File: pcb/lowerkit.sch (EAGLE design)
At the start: 28 parts, among them IC1 MC6847, IC3 74LS93N, IC4 74LS04N, IC5 74LS125N, IC6 74LS86N, IC7 74LS73N, IC8 74LS157N, IC9 74LS157N

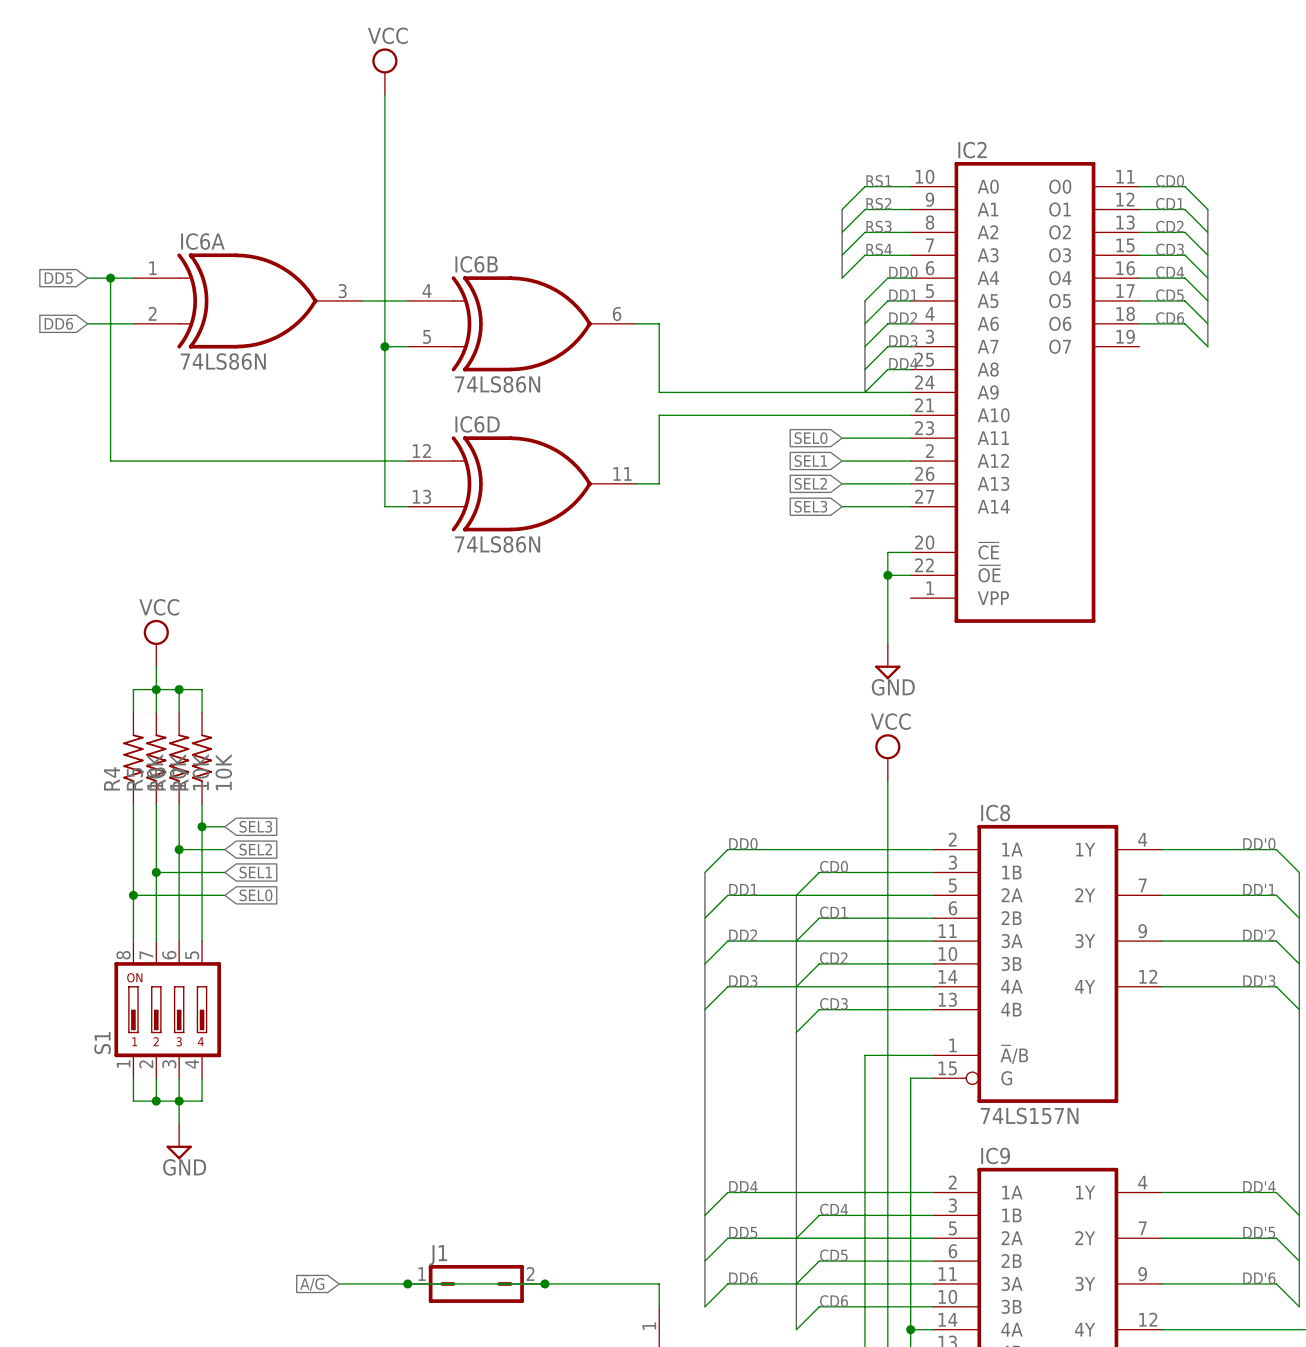
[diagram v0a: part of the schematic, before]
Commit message: Converted original design back to 2716 usage
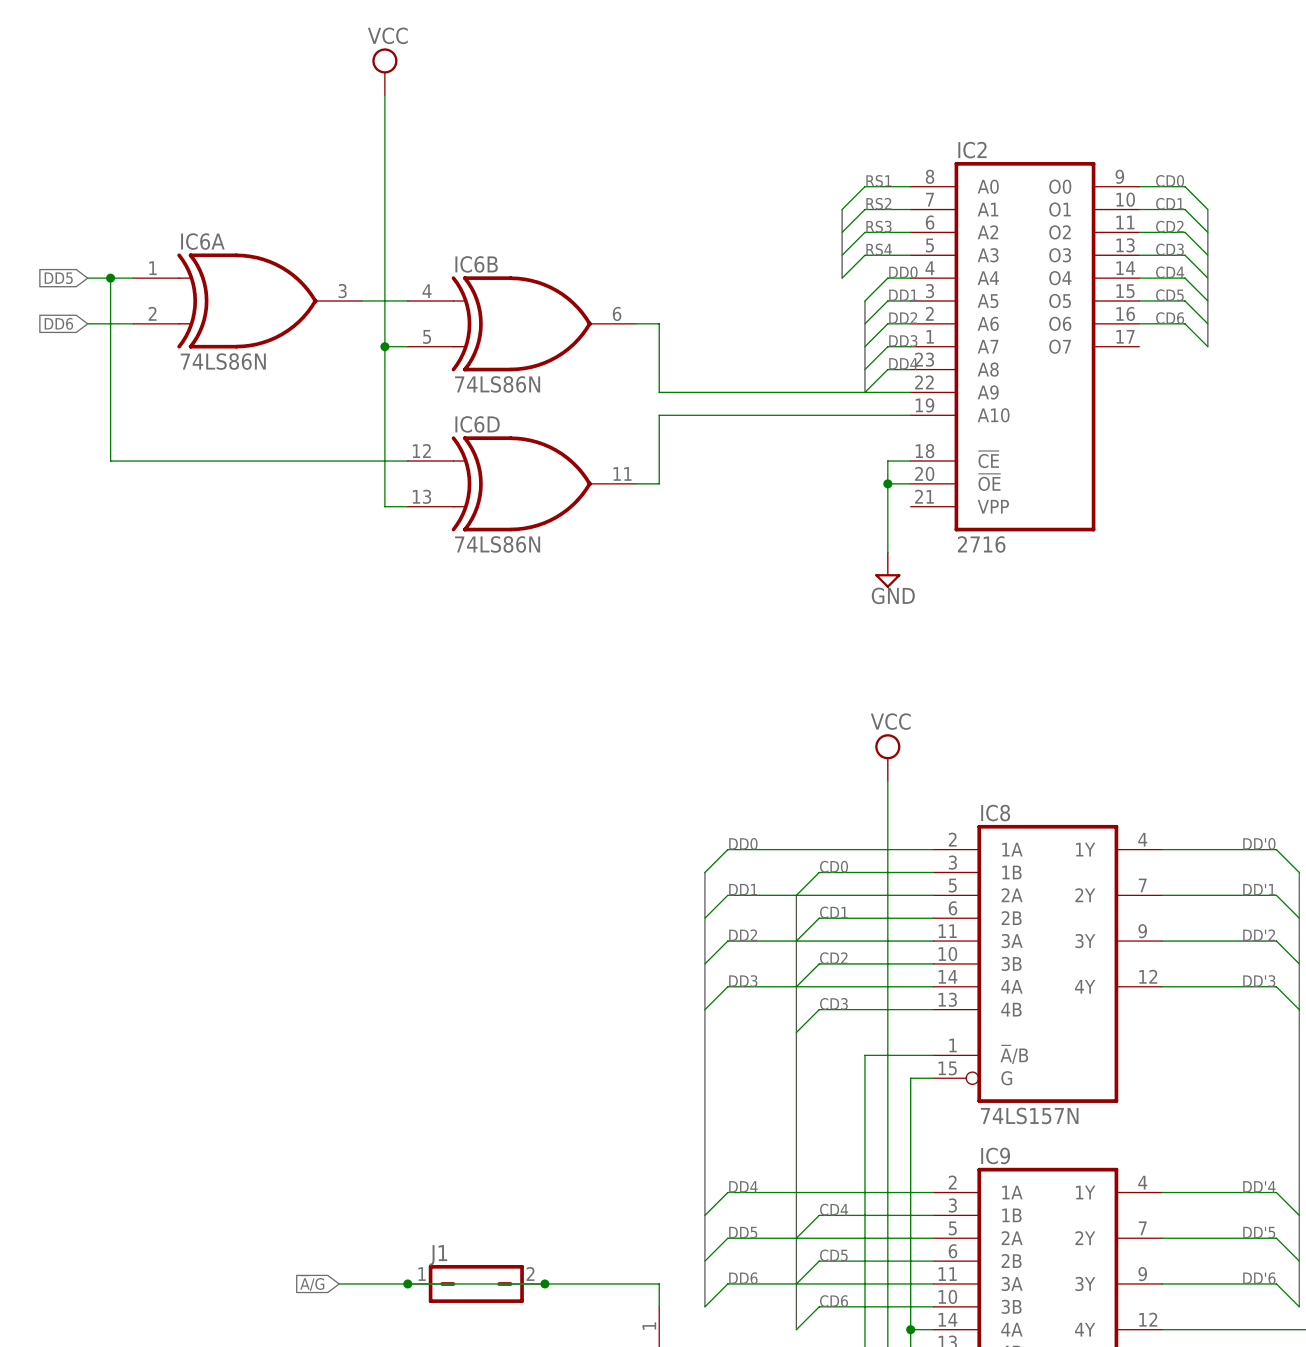
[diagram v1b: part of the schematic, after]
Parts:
- removed R4, R5, R6, R7: 10K, resistor:R-US_0204/7
- removed S1: (no value), switch-dil-rp:DS04
- IC2: value (none) -> 2716; device memory-rp:27256 -> memory-rp:2716
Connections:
- removed net SEL0: IC2A.A11, R4.1, S1.8
- removed net SEL1: IC2A.A12, R5.1, S1.7
- removed net SEL2: IC2A.A13, R6.1, S1.6
- removed net SEL3: IC2A.A14, R7.1, S1.5
- net GND: no longer S1.1, S1.2, S1.3, S1.4
- net VCC: no longer R4.2, R5.2, R6.2, R7.2
